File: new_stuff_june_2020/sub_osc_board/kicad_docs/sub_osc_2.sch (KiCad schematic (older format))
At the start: 22 parts, among them Q3 MMBF4391, Q4 MMBF4391, U4 TL072, U5 TL072, U6 TL072, U7 40106, U8 4013

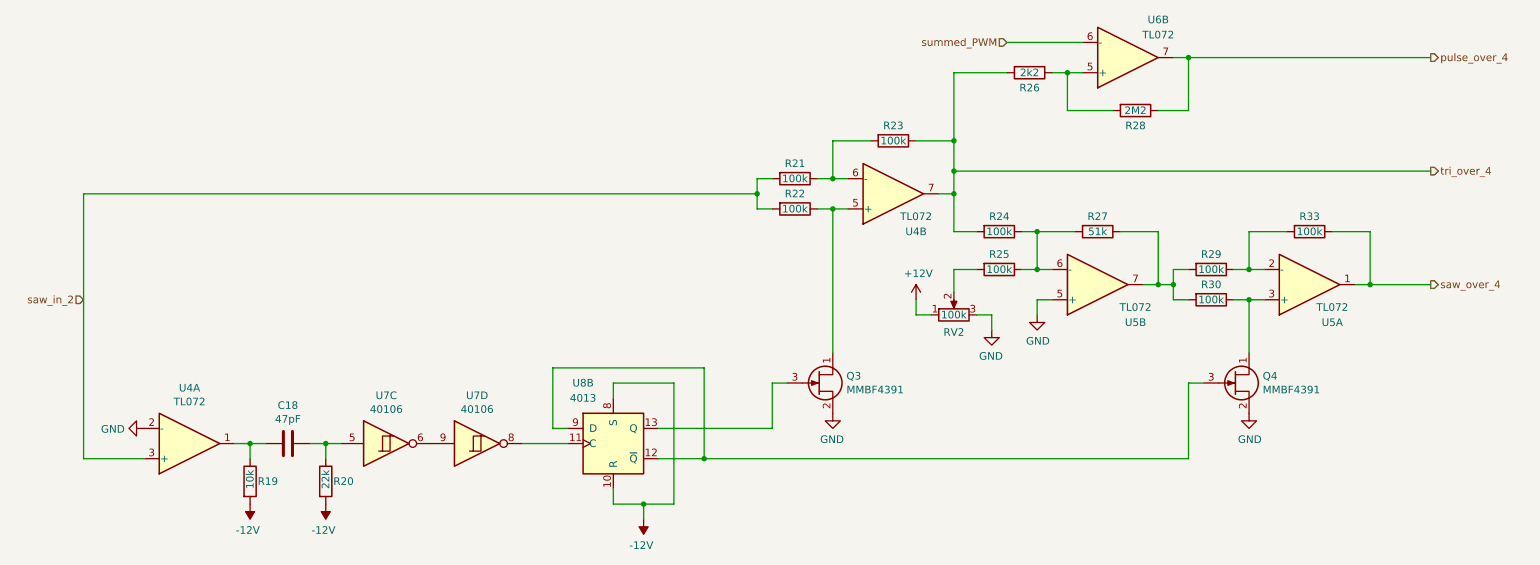
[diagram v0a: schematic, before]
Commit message: change FETs and cap values
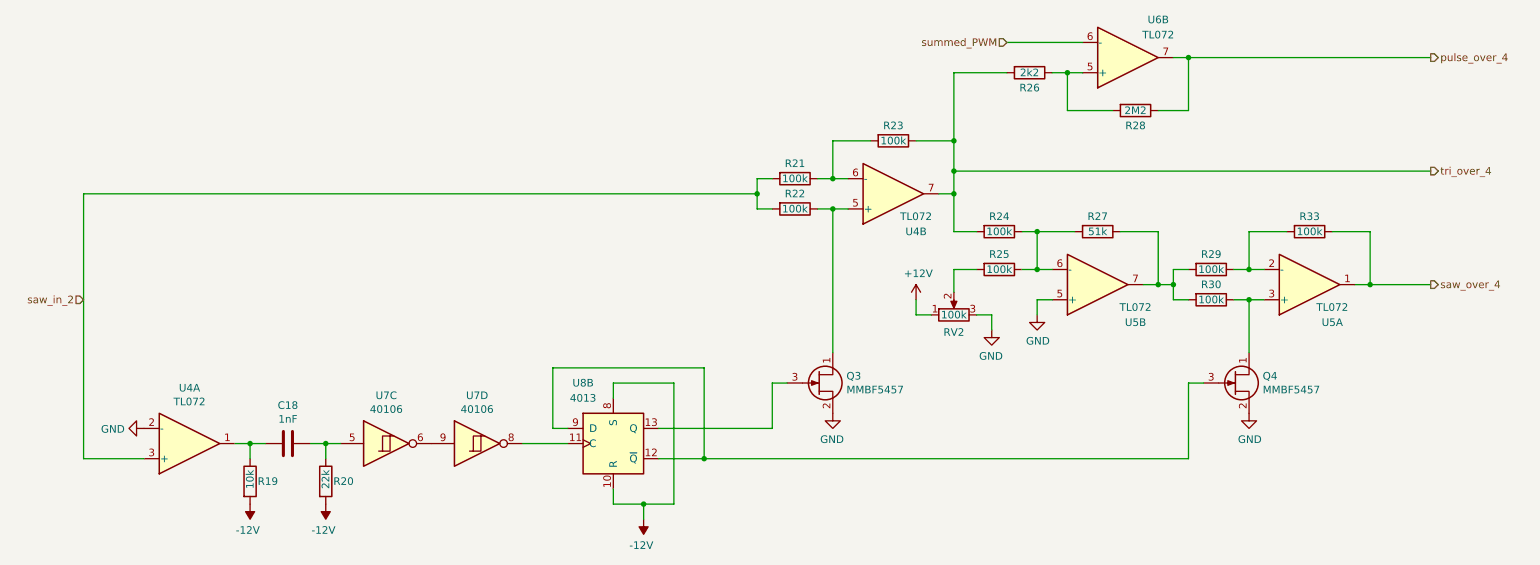
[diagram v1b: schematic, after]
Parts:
- C18: value 47pF -> 1nF
- Q3, Q4: value MMBF4391 -> MMBF5457
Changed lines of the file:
@@
 AR Path="/5EE658F9/5EE8771C" Ref="C18"  Part="1"
 F 0 "C18" V 2598 4200 50  0000 C CNN
-F 1 "47pF" V 2689 4200 50  0000 C CNN
+F 1 "1nF" V 2689 4200 50  0000 C CNN
 F 2 "Capacitor_SMD:C_0805_2012Metric_Pad1.15x1.40mm_HandSolder" H 2888 4050 50  0001 C CNN
 F 3 "~" H 2850 4200 50  0001 C CNN
@@
 P 9100 3800
 F 0 "Q4" H 9290 3846 50  0000 L CNN
-F 1 "MMBF4391" H 9290 3755 50  0000 L CNN
+F 1 "MMBF5457" H 9290 3755 50  0000 L CNN
 F 2 "Package_TO_SOT_SMD:SOT-23_Handsoldering" H 9300 3725 50  0001 L CIN
 F 3 "https://www.onsemi.com/pub/Collateral/MMBF4391LT1-D.PDF" H 9100 3800 50  0001 L CNN
@@
 P 6350 3800
 F 0 "Q3" H 6540 3846 50  0000 L CNN
-F 1 "MMBF4391" H 6540 3755 50  0000 L CNN
+F 1 "MMBF5457" H 6540 3755 50  0000 L CNN
 F 2 "Package_TO_SOT_SMD:SOT-23_Handsoldering" H 6550 3725 50  0001 L CIN
 F 3 "https://www.onsemi.com/pub/Collateral/MMBF4391LT1-D.PDF" H 6350 3800 50  0001 L CNN
